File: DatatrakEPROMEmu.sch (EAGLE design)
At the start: 32 parts, among them IC1 LD1117AS33TR, IC2 XC95144XL_TQ144_P, U1 SN74LVCH16T245DGGR, U2 SN74LVCH16T245DGGR, U3 SN74LVCH16T245DGGR, U4 IS62WV25616DBLL-45TLI, U5 FT240XS, X1 MABC48B2, X2 PN61729-S

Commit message: first routable layout
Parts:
- added X3: (no value), con-molex:22-23-2061
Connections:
- removed net N$1: U3A.1DIR, U3A.2DIR
- new net /TGT_DEN: IC2.PB02_08, U3B.1!OE, U3B.2!OE
- new net A_LV18: IC2.PB04_04
- new net JTCK: IC2.TCK, X3-3.S
- new net JTDI: IC2.TDI, X3-1.S
- new net JTMS: IC2.TMS, X3-2.S
- new net TGT_DIR: IC2.PB02_02, U3A.1DIR, U3A.2DIR
- net +3V3: now also X3-5.S
- net /CE: now also U2A.2B2; no longer U2A.1B5
- net /CE_LV: now also IC2.PB02_10, U2B.2A2; no longer U2B.1A5
- net /OEH: now also U2A.2B5; no longer U2A.1B7
- net /OEH_LV: now also IC2.PB02_06, U2B.2A5; no longer U2B.1A7
- net /OEL: now also U2A.2B4; no longer U2A.1B6
- net /OEL_LV: now also IC2.PB02_11, U2B.2A4; no longer U2B.1A6
- net /PGMH: now also U1A.2B6; no longer U2A.1B4
- net /PGMH_LV: now also IC2.PB04_16, U1B.2A6; no longer U2B.1A4
- net /PGML: now also U1A.2B8; no longer U2A.1B3
- net /PGML_LV: now also IC2.PB06_01, U1B.2A8; no longer U2B.1A3
- net /RAM_CS: now also IC2.PB03_15
- net /RAM_LB: now also IC2.PB01_11
- net /RAM_OE: now also IC2.PB01_09
- net /RAM_UB: now also IC2.PB01_10
- net /RAM_WE: now also IC2.PB00_09
- net A0: now also U2A.2B8; no longer U1A.1B1
- net A1: now also U1A.1B1; no longer U1A.1B2
- net A10: now also U2A.2B3; no longer U1A.2B3
- net A11: now also U2A.2B6; no longer U1A.2B4
- net A12: now also U1A.2B4; no longer U1A.2B5
- net A13: now also U1A.1B5; no longer U1A.2B6
- net A14: now also U1A.1B8; no longer U1A.2B7
- net A15: now also U1A.2B5; no longer U1A.2B8
- net A16: now also U1A.2B7; no longer U2A.1B1
- net A17: now also U1A.2B3; no longer U2A.1B2
- net A4: now also U1A.1B6; no longer U1A.1B5
- net A5: now also U1A.1B7; no longer U1A.1B6
- net A6: now also U1A.2B1; no longer U1A.1B7
- net A7: now also U1A.2B2; no longer U1A.1B8
- net A8: now also U1A.1B2; no longer U1A.2B1
- net A9: now also U2A.2B7; no longer U1A.2B2
- net A_LV0: now also IC2.PB02_14, U2B.2A8; no longer U1B.1A1
- net A_LV1: now also IC2.PB02_16, U1B.1A1; no longer U1B.1A2
- net A_LV10: now also IC2.PB02_03, U2B.2A3; no longer U1B.2A3
- net A_LV11: now also IC2.PB02_09, U2B.2A6; no longer U1B.2A4
- net A_LV12: now also IC2.PB04_06, U1B.2A4; no longer U1B.2A5
- net A_LV13: now also IC2.PB04_07, U1B.1A5; no longer U1B.2A6
- net A_LV14: now also IC2.PB04_02, U1B.1A8; no longer U1B.2A7
- net A_LV15: now also IC2.PB04_09, U1B.2A5; no longer U1B.2A8
- net A_LV16: now also IC2.PB04_12, U1B.2A7; no longer U2B.1A1
- net A_LV17: now also IC2.PB04_14, U1B.2A3; no longer U2B.1A2
- net A_LV3: now also IC2.PB04_05
- net A_LV4: now also IC2.PB04_08, U1B.1A6; no longer U1B.1A5
- net A_LV5: now also IC2.PB04_10, U1B.1A7; no longer U1B.1A6
- net A_LV6: now also IC2.PB04_11, U1B.2A1; no longer U1B.1A7
- net A_LV7: now also IC2.PB04_13, U1B.2A2; no longer U1B.1A8
- net A_LV8: now also IC2.PB04_01, U1B.1A2; no longer U1B.2A1
- net A_LV9: now also IC2.PB02_13, U2B.2A7; no longer U1B.2A2
- net CLK24MHZ: now also IC2.PB02_07
- net D0: now also U3A.2B8; no longer U3A.1B1
- net D1: now also U3A.2B7; no longer U3A.1B2
- net D10: now also U3A.1B5; no longer U3A.2B3
- net D11: now also U3A.1B1; no longer U3A.2B4
- net D12: now also U3A.1B2; no longer U3A.2B5
- net D13: now also U3A.1B3; no longer U3A.2B6
- net D14: now also U3A.1B4; no longer U3A.2B7
- net D15: now also U3A.1B7; no longer U3A.2B8
- net D2: now also U3A.2B6; no longer U3A.1B3
- net D3: now also U3A.2B5; no longer U3A.1B4
- net D4: now also U3A.2B4; no longer U3A.1B5
- net D5: now also U3A.2B3; no longer U3A.1B6
- net D6: now also U3A.2B2; no longer U3A.1B7
- net D7: now also U3A.2B1; no longer U3A.1B8
- net D8: now also U3A.1B8; no longer U3A.2B1
- net D9: now also U3A.1B6; no longer U3A.2B2
- net D_LV0: now also IC2.PB02_01, U3B.2A8, U4.I/O7; no longer U3B.1A1, U4.I/O0
- net D_LV1: now also IC2.PB00_04, U3B.2A7, U4.I/O8; no longer U3B.1A2, U4.I/O1
- net D_LV10: now also IC2.PB01_14, U3B.1A5, U4.I/O13; no longer U3B.2A3, U4.I/O10
- net D_LV11: now also IC2.PB01_13, U3B.1A1, U4.I/O15; no longer U3B.2A4, U4.I/O11
- net D_LV12: now also IC2.PB03_14, U3B.1A2, U4.I/O0; no longer U3B.2A5, U4.I/O12
- net D_LV13: now also IC2.PB01_12, U3B.1A3, U4.I/O14; no longer U3B.2A6, U4.I/O13
- net D_LV14: now also IC2.PB03_12, U3B.1A4, U4.I/O1; no longer U3B.2A7, U4.I/O14
- net D_LV15: now also IC2.PB01_15, U3B.1A7, U4.I/O12; no longer U3B.2A8, U4.I/O15
- net D_LV2: now also IC2.PB02_04, U3B.2A6, U4.I/O6; no longer U3B.1A3, U4.I/O2
- net D_LV3: now also IC2.PB00_02, U3B.2A5, U4.I/O9; no longer U3B.1A4, U4.I/O3
- net D_LV4: now also IC2.PB02_05, U3B.2A4, U4.I/O5; no longer U3B.1A5, U4.I/O4
- net D_LV5: now also IC2.PB00_01, U3B.2A3, U4.I/O10; no longer U3B.1A6, U4.I/O5
- net D_LV6: now also IC2.PB00_15, U3B.2A2, U4.I/O4; no longer U3B.1A7, U4.I/O6
- net D_LV7: now also IC2.PB01_16, U3B.2A1, U4.I/O11; no longer U3B.1A8, U4.I/O7
- net D_LV8: now also U3B.1A8, U4.I/O3; no longer U3B.2A1, U4.I/O8
- net D_LV9: now also IC2.PB03_13, U3B.1A6, U4.I/O2; no longer U3B.2A2, U4.I/O9
- net FTDI_D0: now also IC2.PB07_16
- net FTDI_D1: now also IC2.PB07_13
- net FTDI_D2: now also IC2.PB07_12
- net FTDI_D3: now also IC2.PB07_03
- net FTDI_D4: now also IC2.PB07_14
- net FTDI_D5: now also IC2.PB07_11
- net FTDI_D6: now also IC2.PB07_10
- net FTDI_D7: now also IC2.PB07_09
- net FTDI_RD: now also IC2.PB07_08
- net FTDI_RXF: now also IC2.PB05_01
- net FTDI_TXE: now also IC2.PB07_15
- net FTDI_WR: now also IC2.PB07_02
- net GND: now also IC2.VSSIO_2, U1A.1DIR, U1A.2DIR, U2A.1B1, U2A.1B3, U2A.1B4, U2A.1B5, U2A.1B6, U2A.1B7, U2A.1B8, U2A.2B1, X3-6.S
- net JTDO: now also X3-4.S
- net RAMA0: now also IC2.PB03_16
- net RAMA1: now also IC2.PB01_00
- net RAMA10: now also IC2.PB00_08
- net RAMA11: now also IC2.PB00_00
- net RAMA12: now also IC2.PB00_03
- net RAMA13: now also IC2.PB00_11
- net RAMA14: now also IC2.PB00_13
- net RAMA15: now also IC2.PB00_14
- net RAMA16: now also IC2.PB00_16
- net RAMA17: now also IC2.PB00_10
- net RAMA2: now also IC2.PB01_01
- net RAMA3: now also IC2.PB01_04
- net RAMA4: now also IC2.PB01_05
- net RAMA5: now also IC2.PB01_03
- net RAMA6: now also IC2.PB01_07
- net RAMA7: now also IC2.PB01_08
- net RAMA8: now also IC2.PB00_05
- net RAMA9: now also IC2.PB00_07
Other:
- note added: "JTAG"
- note added: "TODO: Redo RAM <=> FPGA routing. Instead of L/R routing, do half of left pins, all of right pins, then other half of left pins."
- note removed: "TODO: Decoupling caps"
- note removed: "TODO: Route A_LV"
- moved on the sheet: U1B, U2B

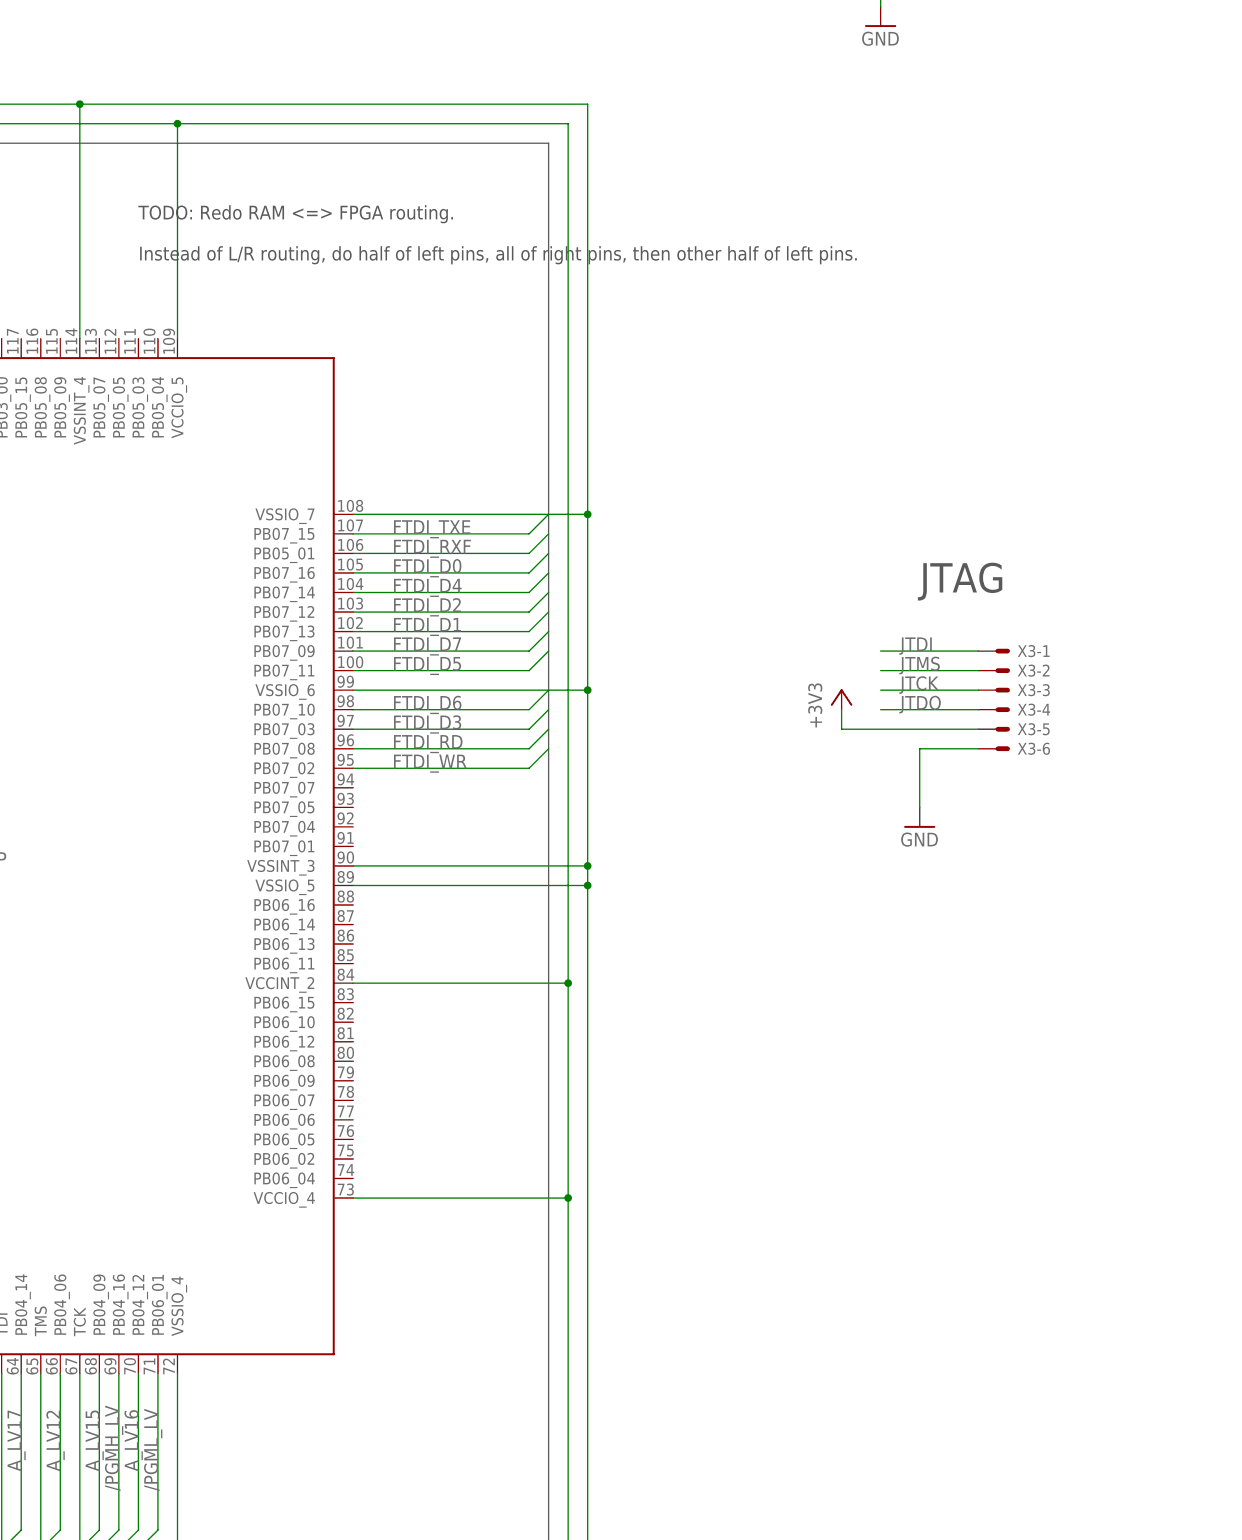
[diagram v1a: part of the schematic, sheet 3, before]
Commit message: add status LEDs
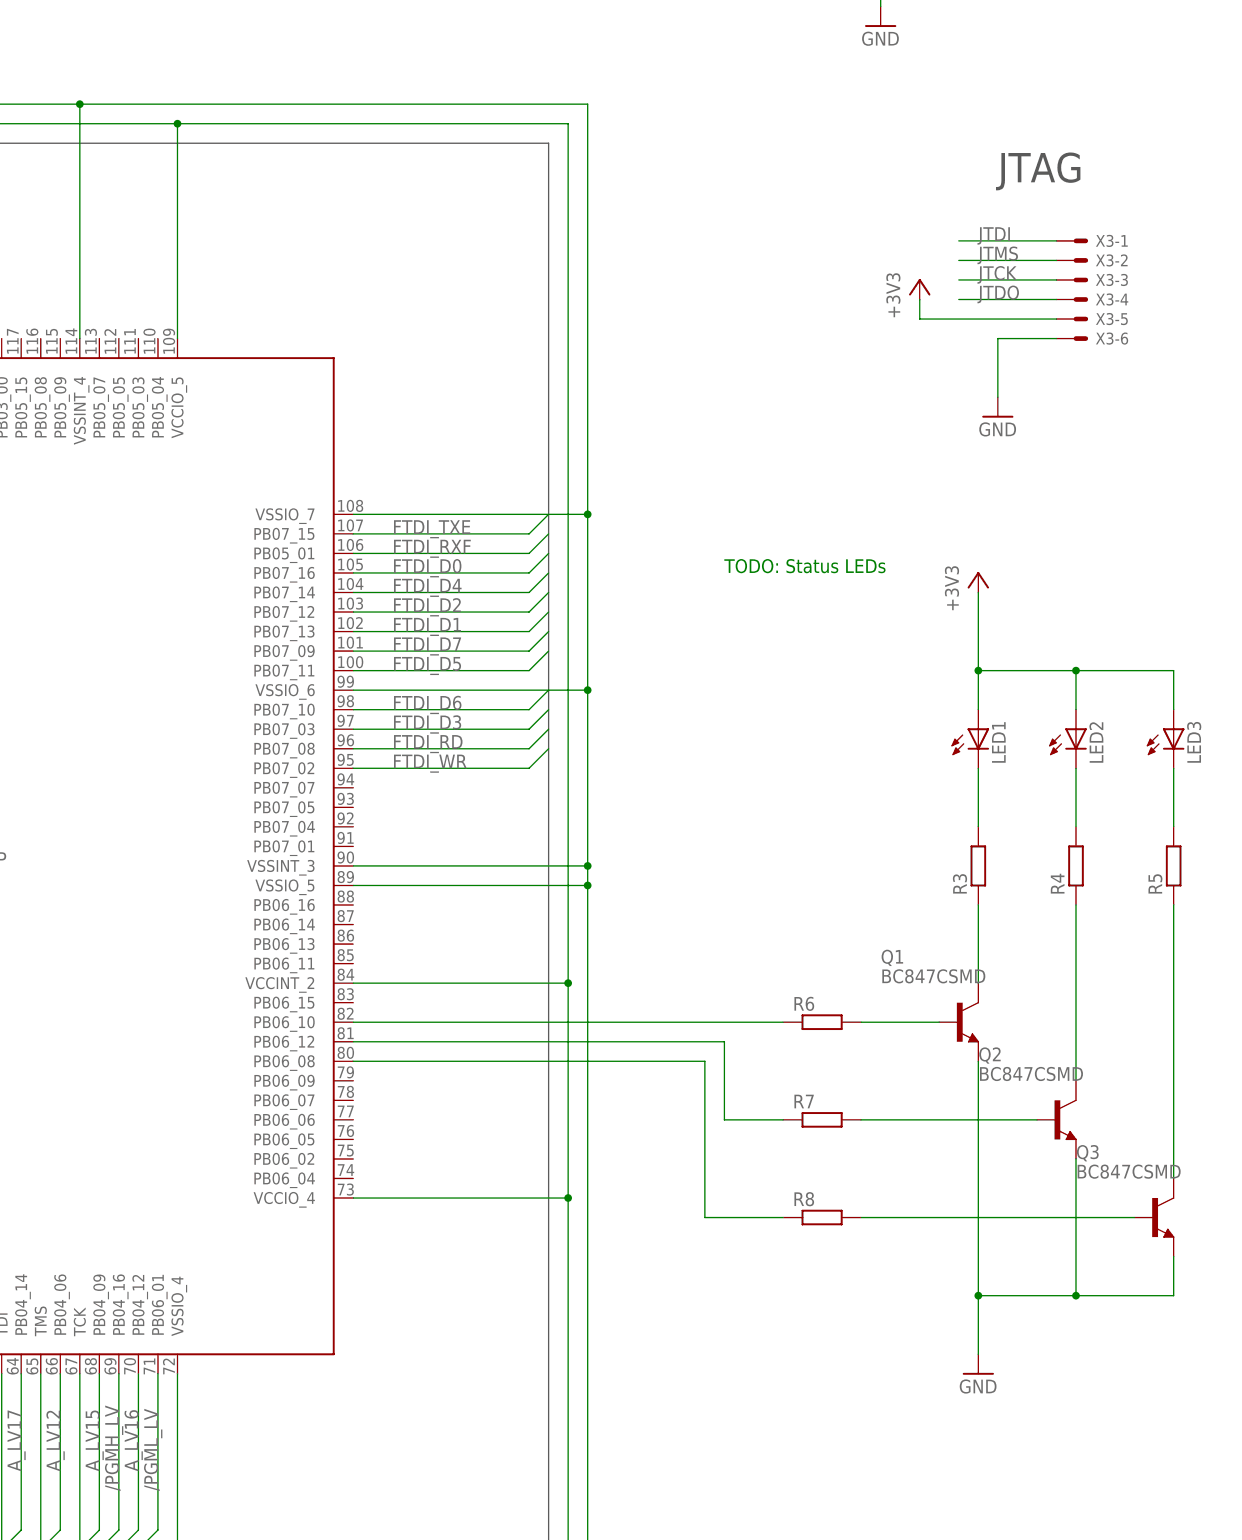
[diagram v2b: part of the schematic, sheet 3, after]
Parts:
- added LED1, LED2, LED3: (no value), led:LEDSML0805
- added Q1, Q2, Q3: BC847CSMD, transistor-npn:BC847CSMD
- added R3, R4, R5, R6, R7, R8: (no value), rcl:R-EU_R0805
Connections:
- new net N$1: Q1.C, R3.1
- new net N$10: Q3.C, R5.1
- new net N$11: LED1.C, R3.2
- new net N$12: LED2.C, R4.2
- new net N$13: LED3.C, R5.2
- new net N$16: IC2.PB06_10, R6.1
- new net N$17: IC2.PB06_12, R7.1
- new net N$18: IC2.PB06_08, R8.1
- new net N$19: Q1.B, R6.2
- new net N$20: Q2.B, R7.2
- new net N$21: Q3.B, R8.2
- new net N$9: Q2.C, R4.1
- net +3V3: now also LED1.A, LED2.A, LED3.A
- net GND: now also Q1.E, Q2.E, Q3.E
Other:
- note added: "TODO: Status LEDs"
- note removed: "TODO: Redo RAM <=> FPGA routing. Instead of L/R routing, do half of left pins, all of right pins, then other half of left pins."
- moved on the sheet: X3-1, X3-2, X3-3, X3-4, X3-5, X3-6

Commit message: fix a few missing routes and ERC errors
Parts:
- C10, C11, C12, C13, C14, C15, C16, C17, C18, C3, C4, C5: value (none) -> 100n
- LED1: value (none) -> RED
- LED2: value (none) -> YELLOW
- LED3: value (none) -> GREEN
- R6, R7, R8: value (none) -> 4k7
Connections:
- removed net A_LV18: IC2.PB04_04
- net A_LV2: now also IC2.PB04_04
- net GND: now also U2A.1B2
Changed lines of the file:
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@@
 <part name="C1" library="rcl" deviceset="C-EU" device="C0805" value="100n"/>
 <part name="C2" library="rcl" deviceset="C-EU" device="C0805" value="10u"/>
-<part name="C3" library="rcl" deviceset="C-EU" device="C0805"/>
-<part name="C4" library="rcl" deviceset="C-EU" device="C0805"/>
-<part name="C5" library="rcl" deviceset="C-EU" device="C0805"/>
+<part name="C3" library="rcl" deviceset="C-EU" device="C0805" value="100n"/>
+<part name="C4" library="rcl" deviceset="C-EU" device="C0805" value="100n"/>
+<part name="C5" library="rcl" deviceset="C-EU" device="C0805" value="100n"/>
 <part name="+3V4" library="supply1" deviceset="+3V3" device=""/>
 <part name="GND10" library="supply1" deviceset="GND" device=""/>
@@
 <part name="GND18" library="supply1" deviceset="GND" device=""/>
 <part name="C9" library="rcl" deviceset="C-EU" device="C0805" value="100n"/>
-<part name="C10" library="rcl" deviceset="C-EU" device="C0805"/>
-<part name="C11" library="rcl" deviceset="C-EU" device="C0805"/>
-<part name="C12" library="rcl" deviceset="C-EU" device="C0805"/>
-<part name="C13" library="rcl" deviceset="C-EU" device="C0805"/>
-<part name="C14" library="rcl" deviceset="C-EU" device="C0805"/>
-<part name="C15" library="rcl" deviceset="C-EU" device="C0805"/>
-<part name="C16" library="rcl" deviceset="C-EU" device="C0805"/>
-<part name="C17" library="rcl" deviceset="C-EU" device="C0805"/>
-<part name="C18" library="rcl" deviceset="C-EU" device="C0805"/>
+<part name="C10" library="rcl" deviceset="C-EU" device="C0805" value="100n"/>
+<part name="C11" library="rcl" deviceset="C-EU" device="C0805" value="100n"/>
+<part name="C12" library="rcl" deviceset="C-EU" device="C0805" value="100n"/>
+<part name="C13" library="rcl" deviceset="C-EU" device="C0805" value="100n"/>
+<part name="C14" library="rcl" deviceset="C-EU" device="C0805" value="100n"/>
+<part name="C15" library="rcl" deviceset="C-EU" device="C0805" value="100n"/>
+<part name="C16" library="rcl" deviceset="C-EU" device="C0805" value="100n"/>
+<part name="C17" library="rcl" deviceset="C-EU" device="C0805" value="100n"/>
+<part name="C18" library="rcl" deviceset="C-EU" device="C0805" value="100n"/>
 <part name="+3V5" library="supply1" deviceset="+3V3" device=""/>
 <part name="GND19" library="supply1" deviceset="GND" device=""/>
@@
 <part name="Q2" library="transistor-npn" deviceset="BC847*" device="SMD" technology="C"/>
 <part name="Q3" library="transistor-npn" deviceset="BC847*" device="SMD" technology="C"/>
-<part name="LED1" library="led" deviceset="LED" device="SML0805"/>
-<part name="LED2" library="led" deviceset="LED" device="SML0805"/>
-<part name="LED3" library="led" deviceset="LED" device="SML0805"/>
+<part name="LED1" library="led" deviceset="LED" device="SML0805" value="RED"/>
+<part name="LED2" library="led" deviceset="LED" device="SML0805" value="YELLOW"/>
+<part name="LED3" library="led" deviceset="LED" device="SML0805" value="GREEN"/>
 <part name="R3" library="rcl" deviceset="R-EU_" device="R0805"/>
 <part name="R4" library="rcl" deviceset="R-EU_" device="R0805"/>
@@
 <part name="+3V10" library="supply1" deviceset="+3V3" device=""/>
 <part name="GND24" library="supply1" deviceset="GND" device=""/>
-<part name="R6" library="rcl" deviceset="R-EU_" device="R0805"/>
-<part name="R7" library="rcl" deviceset="R-EU_" device="R0805"/>
-<part name="R8" library="rcl" deviceset="R-EU_" device="R0805"/>
+<part name="R6" library="rcl" deviceset="R-EU_" device="R0805" value="4k7"/>
+<part name="R7" library="rcl" deviceset="R-EU_" device="R0805" value="4k7"/>
+<part name="R8" library="rcl" deviceset="R-EU_" device="R0805" value="4k7"/>
 </parts>
 <sheets>
@@
 <wire x1="210.82" y1="215.9" x2="215.9" y2="215.9" width="0.1524" layer="91"/>
 <junction x="210.82" y="215.9"/>
-<wire x1="215.9" y1="218.44" x2="210.82" y2="218.44" width="0.1524" layer="91"/>
-<junction x="210.82" y="218.44"/>
 <pinref part="U2" gate="A" pin="1B1"/>
 <wire x1="210.82" y1="220.98" x2="215.9" y2="220.98" width="0.1524" layer="91"/>
 <junction x="210.82" y="220.98"/>
+<pinref part="U2" gate="A" pin="1B2"/>
+<wire x1="215.9" y1="218.44" x2="210.82" y2="218.44" width="0.1524" layer="91"/>
+<junction x="210.82" y="218.44"/>
 </segment>
 <segment>
@@
 </segment>
 </net>
-<net name="A_LV18" class="0">
-<segment>
-<wire x1="172.72" y1="53.34" x2="172.72" y2="33.02" width="0.1524" layer="91"/>
-<wire x1="172.72" y1="33.02" x2="170.18" y2="30.48" width="0.1524" layer="91"/>
-<label x="172.72" y="40.64" size="1.778" layer="95" rot="R90"/>
-<pinref part="IC2" gate="G$1" pin="PB04_04"/>
-</segment>
-</net>
 <net name="A_LV8" class="0">
 <segment>
@@
 </segment>
 </net>
+<net name="A_LV2" class="0">
+<segment>
+<pinref part="IC2" gate="G$1" pin="PB04_04"/>
+<wire x1="172.72" y1="53.34" x2="172.72" y2="33.02" width="0.1524" layer="91"/>
+<wire x1="172.72" y1="33.02" x2="170.18" y2="30.48" width="0.1524" layer="91"/>
+<label x="172.72" y="40.64" size="1.778" layer="95" rot="R90"/>
+</segment>
+</net>
